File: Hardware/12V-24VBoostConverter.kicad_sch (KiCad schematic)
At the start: 19 parts, among them IC1 TPS613771RYHR, U2 3568

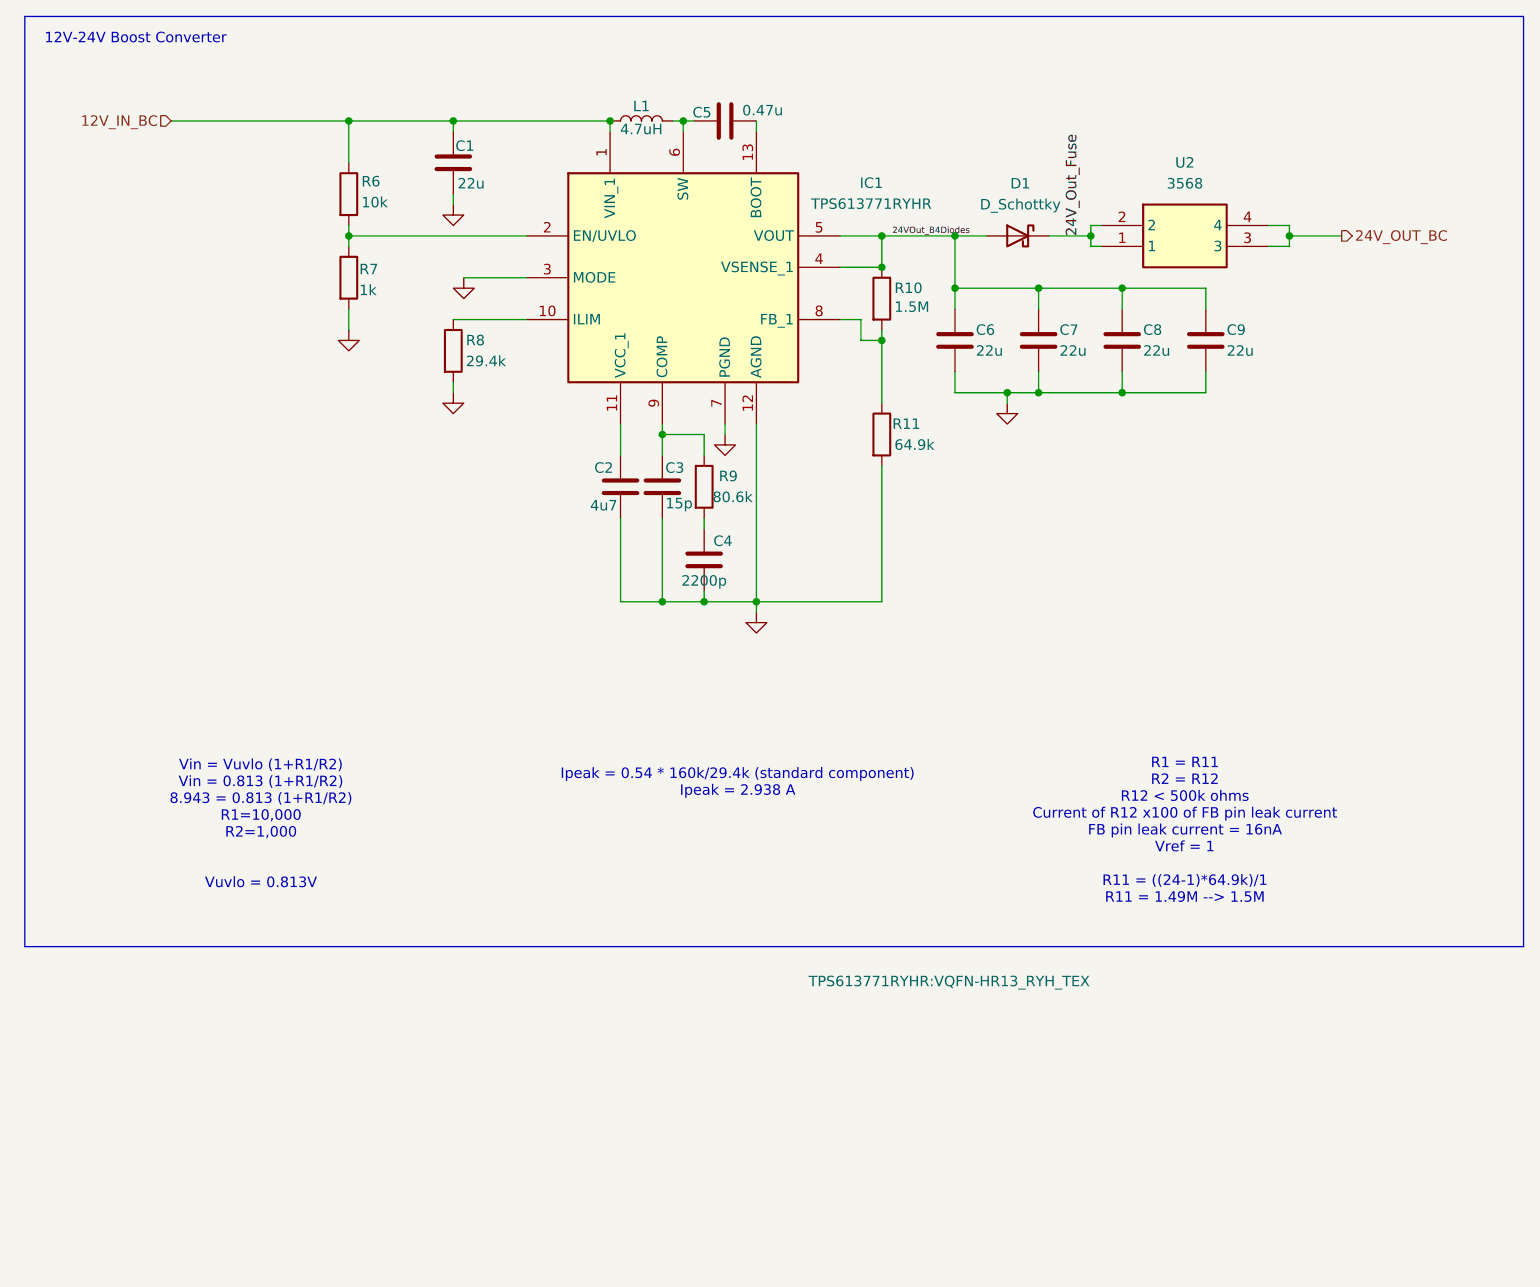
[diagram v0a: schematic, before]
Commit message: Bring Hardware folder from RevB
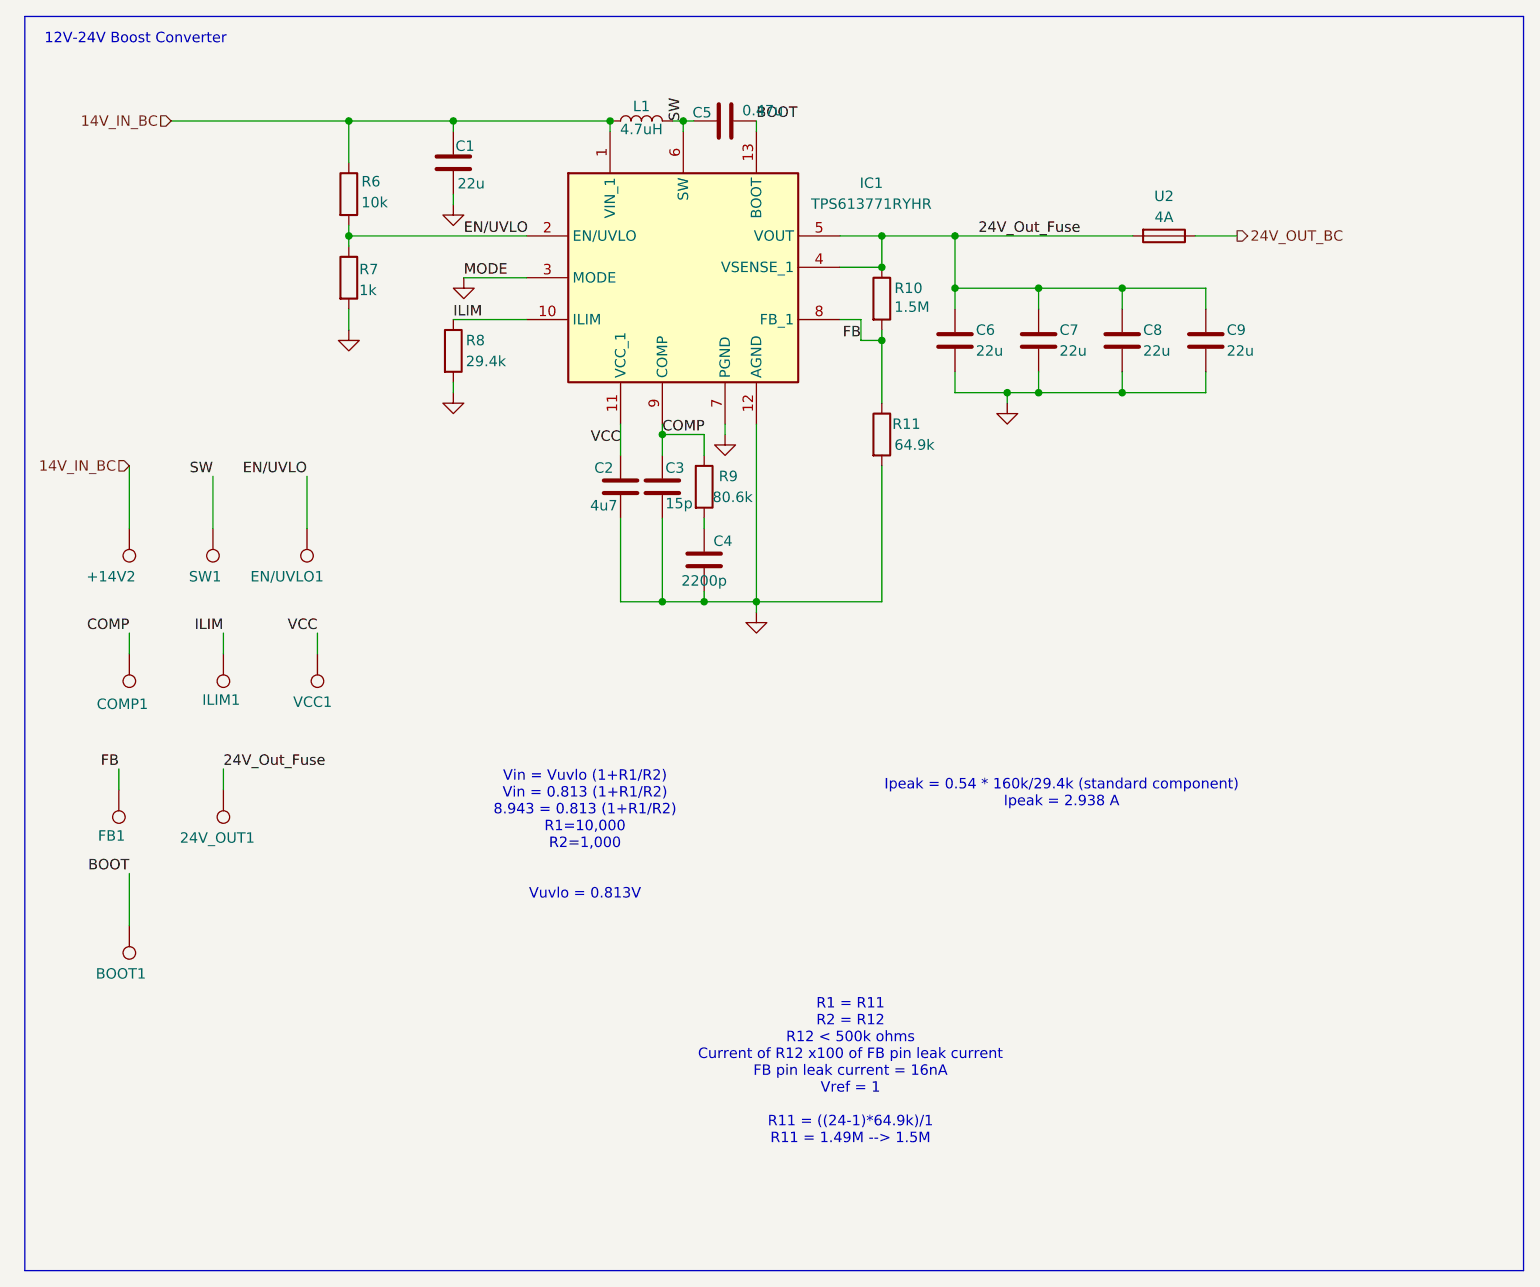
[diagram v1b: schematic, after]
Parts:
- removed D1: D_Schottky, SK32A_LTP:SDO_DO-214AC-SMA_MCE, symbol Device:D_Schottky
- added +14V2, 24V_OUT1: TestPoint, TestPoint:TestPoint_THTPad_D3.0mm_Drill1.5mm, symbol Connector:TestPoint
- added BOOT1, COMP1, EN/UVLO1, FB1, ILIM1, SW1, VCC1: TestPoint, TestPoint:TestPoint_THTPad_D1.5mm_Drill0.7mm, symbol Connector:TestPoint
- C4: P/N GCJ188R71E222KA01D -> 0603B222K500NT
- L1: footprint XGL4020-472MEC:IND_XGL4020_COC -> charger_parts:XGL4020_COC
- R6: P/N CRCW060310K0FKEI -> CRCW060310K0FKEI
- U2: value 3568 -> 4A; symbol 3568:3568 -> Device:Fuse; Manufacturer_Part_Number (none) -> 3568
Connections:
- net 24VOut_B4Diodes is gone; now on net 24V_Out_Fuse: C6.1, C7.1, C8.1, C9.1, IC1.4 (VSENSE_1), IC1.5 (VOUT), R10.1
- net 24V_OUT_BC: now also U2.1; no longer U2.3, U2.4
- net 24V_Out_Fuse: now also 24V_OUT1.1; no longer U2.1
- net VCC: now reaches C2.2, IC1.11 (VCC_1)
- net VCC: now also VCC1.1
- net COMP: now reaches C3.2, IC1.9 (COMP), R9.1
- net COMP: now also COMP1.1
- net EN/UVLO: now reaches IC1.2 (EN/UVLO), R6.2, R7.1
- net EN/UVLO: now also EN/UVLO1.1
- net FB: now reaches IC1.8 (FB_1), R10.2, R11.1
- net FB: now also FB1.1
- net SW: now reaches C5.1, IC1.6 (SW), L1.2
- net SW: now also SW1.1
- net ILIM: now reaches IC1.10 (ILIM), R8.1
- net ILIM: now also ILIM1.1
- net BOOT: now reaches C5.2, IC1.13 (BOOT)
- net BOOT: now also BOOT1.1
- net 12V_IN_BC renamed 14V_IN_BC
- net 14V_IN_BC: now also +14V2.1
